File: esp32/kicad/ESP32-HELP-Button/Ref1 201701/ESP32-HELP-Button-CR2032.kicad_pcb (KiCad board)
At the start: 2 copper layers, 45 x 26 mm, 34 parts, among them P1 CONN_01X05, Q1 Q_NMOS_GDS, SW1 SW_PUSH, U1 ES-WROOM-32

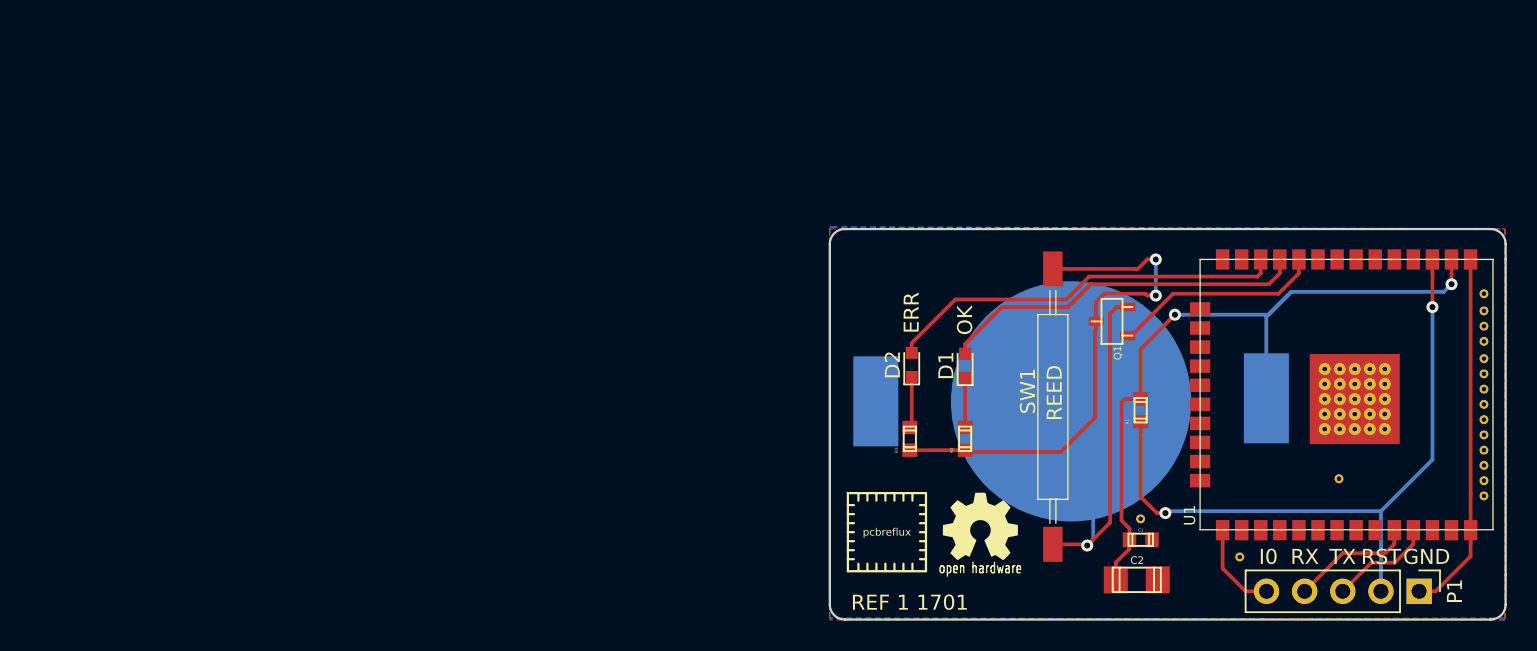
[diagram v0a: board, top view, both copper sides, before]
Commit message: ESP32-HELP-Button
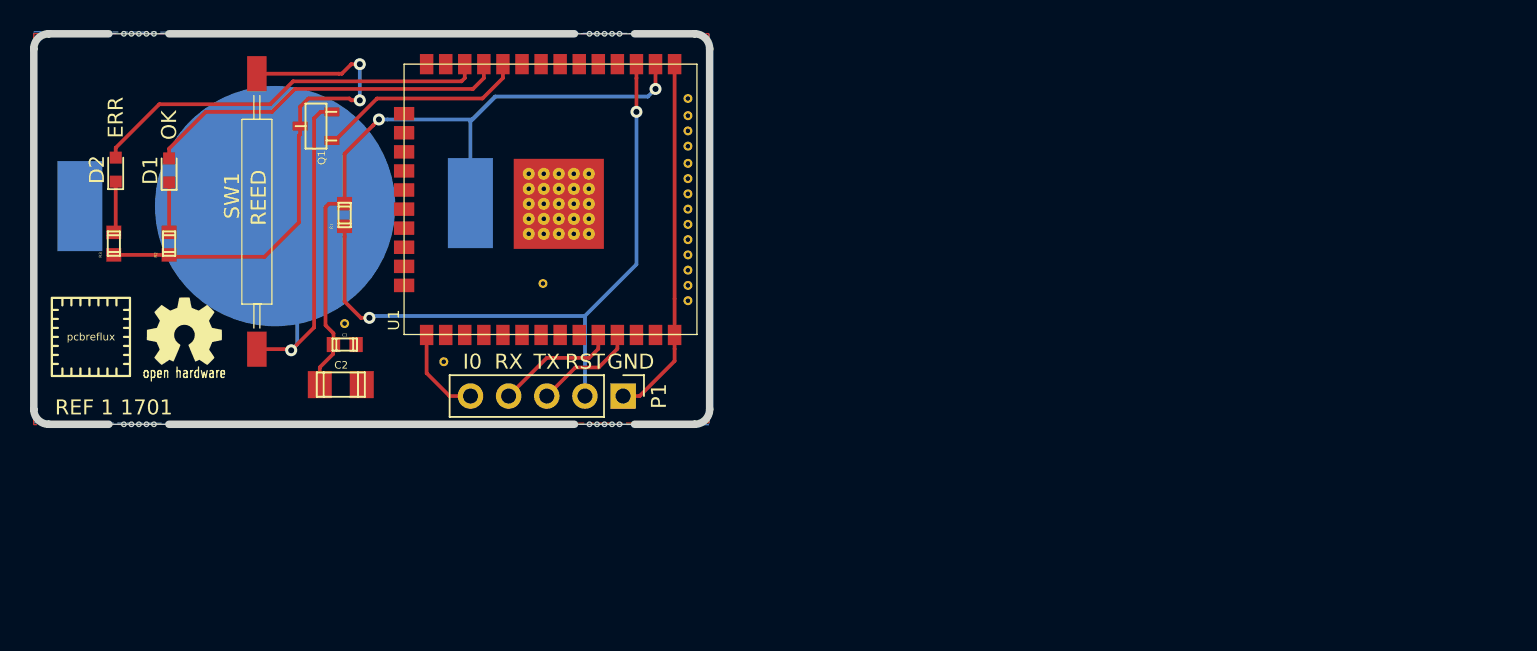
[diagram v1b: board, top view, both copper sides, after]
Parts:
- added REF**: micro_bite, module:micro_bite, F.Cu at (33.0, 34.0)
- added REF**: micro_bite, module:micro_bite, F.Cu at (33.0, 60.0)
- added REF**: micro_bite, module:micro_bite, F.Cu at (64.0, 60.0)
- added REF**: micro_bite, module:micro_bite, F.Cu at (64.0, 34.0)
- moved C1 54.6 mm to (46.7, 54.7)
- moved Q1 54.6 mm to (44.8, 40.1)
- moved REF** 54.6 mm to (53.3, 55.8)
- moved REF** 54.6 mm to (59.9, 50.6)
- moved U1 54.6 mm to (50.7, 36.0)
- moved BT1 54.6 mm to (42.1, 45.5)
- moved C2 54.6 mm to (46.4, 57.4)
- moved D2 54.6 mm to (31.5, 43.0)
- moved G*** 54.6 mm to (29.9, 36.9)
- moved G*** 54.6 mm to (36.0, 53.8)
- moved P1 54.6 mm to (65.2, 58.1)
- moved R3 54.6 mm to (31.3, 48.0)
- moved REF** 54.6 mm to (69.6, 47.7)
- moved REF** 54.6 mm to (69.6, 46.7)
- moved REF** 54.6 mm to (69.6, 45.7)
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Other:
- outline, holes or cut-outs redrawn
